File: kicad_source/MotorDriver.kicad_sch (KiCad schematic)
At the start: 52 parts, among them J19 S6B-XH-A, J20 S6B-XH-A, J7 x, J8 x, J9 x, Q1 2N7002, U4 74xx08, U5 IFX007T, U6 IFX007T, U7 IFX007T, U8 IFX007T

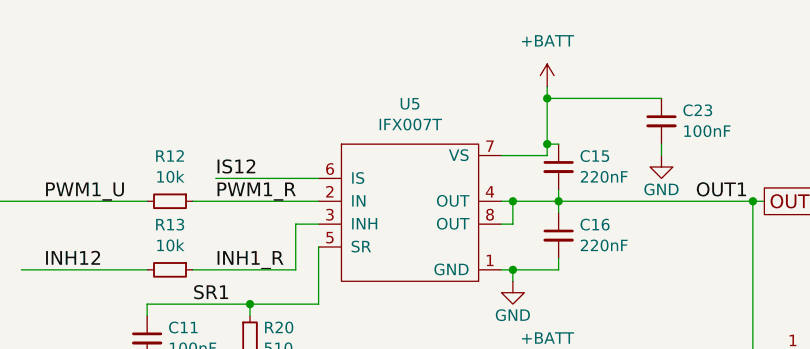
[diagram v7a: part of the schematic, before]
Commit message: checked supply voltage of parts
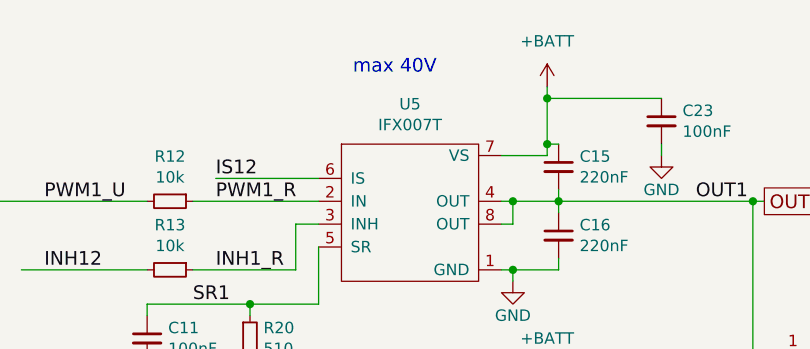
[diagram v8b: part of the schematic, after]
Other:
- note added: "max 40V"
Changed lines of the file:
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@@
     (stroke (width 0) (type default) (color 0 0 0 0))
+  )
+  (text "max 40V" (at 200.66 20.32 0)
+    (effects (font (size 1.524 1.524)) (justify left bottom))
   )
   (label "PWM2_U" (at 166.37 67.31 0)
